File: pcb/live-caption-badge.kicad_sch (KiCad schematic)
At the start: 33 parts, among them J1 USB_C_Receptacle_USB2.0_14P, J2 Conn_01x04_Socket, J3 Conn_01x08_Socket, SW1 KILL, SW2 RST, SW3 BTN, SW4 BTN, SW5 BTN, U1 ESP32-S3-WROOM-1, U2 HE9073A33M5R, U3 HE9073A33M5R

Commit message: pcb: More layout, design 18650 battery holder footprint
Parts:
- BT1: footprint (none) -> live-caption-badge:BH-18650-B1BA002
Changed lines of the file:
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@@
 			)
 		)
-		(property "Footprint" ""
+		(property "Footprint" "live-caption-badge:BH-18650-B1BA002"
 			(at 50.8 49.276 90)
 			(effects

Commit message: pcb: I'm working in Spain but the S is silent
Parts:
- removed J1: USB_C_Receptacle_USB2.0_14P, symbol Connector:USB_C_Receptacle_USB2.0_14P
- removed J3: Conn_01x08_Socket, Connector_PinSocket_2.00mm:PinSocket_1x08_P2.00mm_Horizontal, symbol Connector:Conn_01x08_Socket
- added J3: Conn_01x09, Connector_Molex:Molex_CLIK-Mate_502386-0970_1x09-1MP_P1.25mm_Horizontal, symbol Connector_Generic:Conn_01x09
- added J5: USB_C_Receptacle_USB2.0_16P, live-caption-badge:USB_C_Receptacle_Molex_2169900002, symbol Connector:USB_C_Receptacle_USB2.0_16P
- SW3, SW4, SW5: footprint (none) -> live-caption-badge:SW_Push_TL1100CF160Q
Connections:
- net +3V3: now also J3.1 (Pin_1)
- net EPD_DC: now also J3.6 (Pin_6)
- net EPD_~{BUSY}: now also J3.8 (Pin_8)
- net EPD_~{RST}: now also J3.7 (Pin_7)
- net GND: now also J3.2 (Pin_2), J5.A1 (GND), J5.A12 (GND), J5.B1 (GND), J5.B12 (GND), J5.S1 (SHIELD)
- net SPI_CS: now also J3.5 (Pin_5)
- net SPI_MOSI: now also J3.3 (Pin_3)
- net SPI_SCK: now also J3.4 (Pin_4)
- net USB_D+: now also J5.A6 (D+), J5.B6 (D+)
- net USB_D-: now also J5.A7 (D-), J5.B7 (D-)
- net VBUS: now also J5.A4 (VBUS), J5.A9 (VBUS), J5.B4 (VBUS), J5.B9 (VBUS)
- net at R5.1: now also J5.B5 (CC2)
- net at R4.1: now also J5.A5 (CC1)
- net EPD_PWR: now reaches U1.7 (IO7)
- net EPD_PWR: now also J3.9 (Pin_9)
- no-connect marks 15 -> 16
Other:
- note added: "5V"

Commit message: pcb: 473 cannot defeat me in any way that matters
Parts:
- removed C5, C6: TBD, Capacitor_SMD:C_0603_1608Metric, symbol Device:C_Small
- removed R6, R7: 0, Resistor_SMD:R_0603_1608Metric, symbol Device:R_US
- removed SW1: KILL, symbol Switch:SW_SPDT
- added J3: Conn_01x09, Connector_PinHeader_2.54mm:PinHeader_1x09_P2.54mm_Vertical, symbol Connector_Generic:Conn_01x09
- added SW1: SW_DPDT_x2, live-caption-badge:SW_DPDT_SLW-867569-4A-N-D, symbol Switch:SW_DPDT_x2
- SW2: footprint (none) -> live-caption-badge:SW_Push_6x3mm
- renumbered J3 to J1
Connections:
- net +3V3: now also J3.1 (Pin_1)
- net +BATT: now also BT1.1 (+), SW1.1 (A); no longer C7.1, C9.1, U2.1 (IN), U2.3 (CE), U3.1 (IN), U3.3 (CE)
- net EPD_DC: now also J3.6 (Pin_6)
- net EPD_PWR: now also J3.9 (Pin_9)
- net EPD_~{BUSY}: now also J3.8 (Pin_8)
- net EPD_~{RST}: now also J3.7 (Pin_7)
- net GND: now also J3.2 (Pin_2)
- net SPI_CS: now also J3.5 (Pin_5)
- net SPI_MOSI: now also J3.3 (Pin_3)
- net SPI_SCK: now also J3.4 (Pin_4)
- net USB_D+: now also U1.14 (IO20)
- net USB_D-: now also U1.13 (IO19)
- net VBUS: now also SW1.3 (C)
- new net V_UNREG: C7.1, C9.1, SW1.2 (B), U2.1 (IN), U2.3 (CE), U3.1 (IN), U3.3 (CE)
- no-connect marks 16 -> 18
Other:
- note removed: "In case we need some lowpassing"
- moved on the sheet: BT1, C11, C12, C13, J2, R8, SW3, SW4, SW5

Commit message: pcb: pretty much done
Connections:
- net ADC_INT: now also U1.27 (IO0); no longer U1.16 (IO46)
- net AMP_CTRL: now also U1.38 (IO2); no longer U1.25 (IO48)
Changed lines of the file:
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@@
-	)
-	(no_connect
-		(at 124.46 45.72)
 	)
 	(no_connect
@@
 	)
 	(no_connect
+		(at 154.94 81.28)
+	)
+	(no_connect
 		(at 154.94 55.88)
 	)
@@
 	)
 	(no_connect
-		(at 124.46 50.8)
+		(at 154.94 86.36)
 	)
 	(no_connect
@@
 	(wire
 		(pts
-			(xy 154.94 86.36) (xy 165.1 86.36)
+			(xy 124.46 50.8) (xy 114.3 50.8)
 		)
 		(stroke
@@
 	(wire
 		(pts
-			(xy 154.94 81.28) (xy 165.1 81.28)
+			(xy 124.46 45.72) (xy 114.3 45.72)
 		)
 		(stroke
@@
 	)
 	(label "ADC_INT"
-		(at 165.1 81.28 180)
-		(fields_autoplaced yes)
-		(effects
-			(font
-				(size 1.27 1.27)
-			)
-			(justify right bottom)
+		(at 114.3 45.72 0)
+		(fields_autoplaced yes)
+		(effects
+			(font
+				(size 1.27 1.27)
+			)
+			(justify left bottom)
 		)
 	)
@@
 	)
 	(label "AMP_CTRL"
-		(at 165.1 86.36 180)
-		(fields_autoplaced yes)
-		(effects
-			(font
-				(size 1.27 1.27)
-			)
-			(justify right bottom)
-		)
-	)
+		(at 114.3 50.8 0)
+		(fields_autoplaced yes)
+		(effects
+			(font
+				(size 1.27 1.27)
+			)
+			(justify left bottom)
+		)
+	)

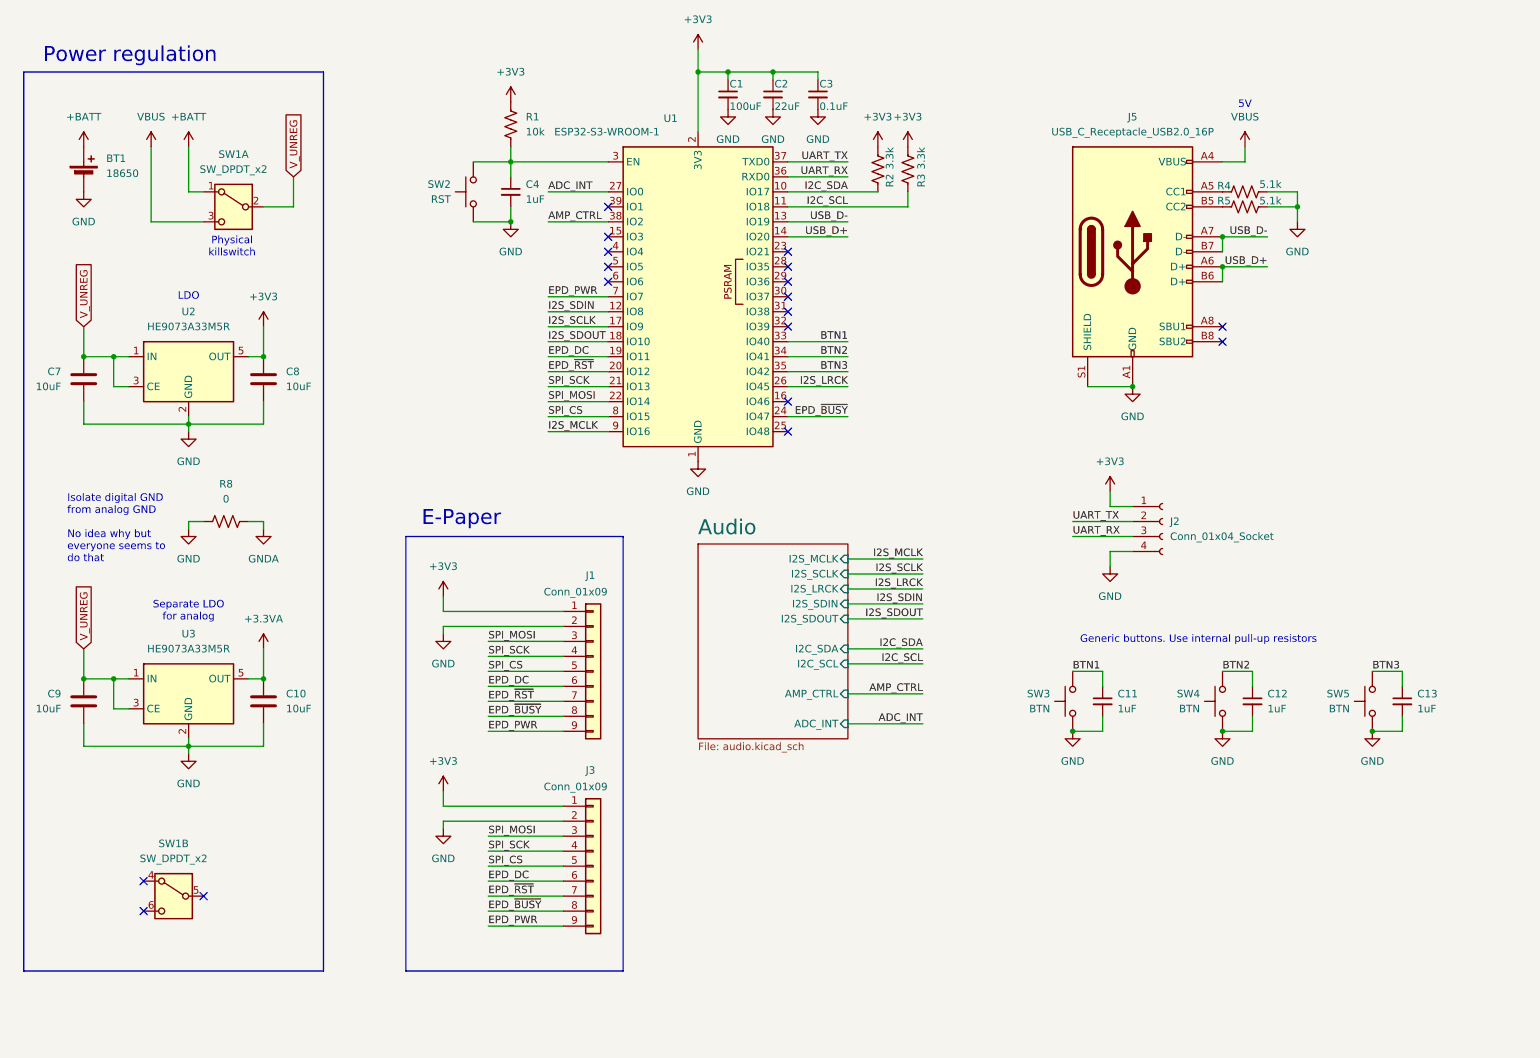
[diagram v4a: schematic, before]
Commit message: pcb: Fix misc footprints, add silkprint
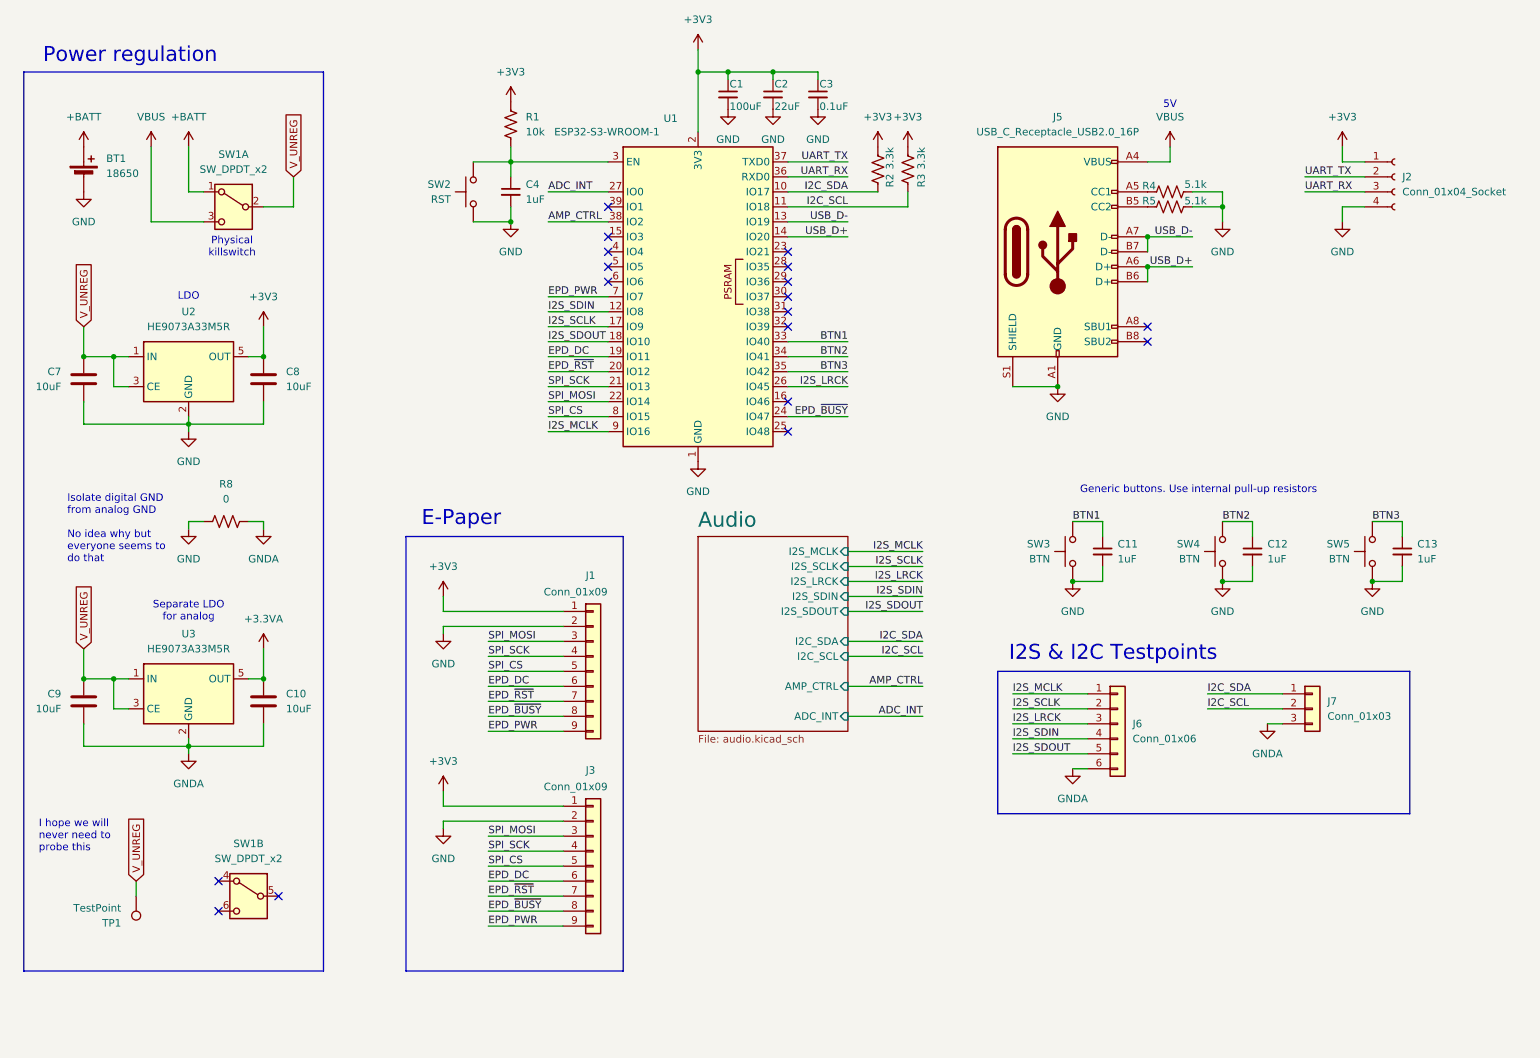
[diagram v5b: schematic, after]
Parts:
- added J6: Conn_01x06, Connector_PinHeader_2.54mm:PinHeader_1x06_P2.54mm_Vertical, symbol Connector_Generic:Conn_01x06
- added J7: Conn_01x03, Connector_PinHeader_2.54mm:PinHeader_1x03_P2.54mm_Vertical, symbol Connector_Generic:Conn_01x03
- added TP1: TestPoint, symbol Connector:TestPoint
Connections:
- net GND: no longer C10.2, C9.2, U3.2 (GND)
- net GNDA: now also C10.2, C9.2, U3.2 (GND), J6.6 (Pin_6), J7.3 (Pin_3)
- net I2C_SCL: now also J7.2 (Pin_2)
- net I2C_SDA: now also J7.1 (Pin_1)
- net I2S_LRCK: now also J6.3 (Pin_3)
- net I2S_MCLK: now also J6.1 (Pin_1)
- net I2S_SCLK: now also J6.2 (Pin_2)
- net I2S_SDIN: now also J6.4 (Pin_4)
- net I2S_SDOUT: now also J6.5 (Pin_5)
- net V_UNREG: now also TP1.1
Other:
- note added: "I hope we will never need to probe this"
- note added: "I2S & I2C Testpoints"
- moved on the sheet: C11, C12, C13, J2, J5, R4, R5, SW1B, SW3, SW4, SW5

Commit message: pcb: Checkpoint before incorporating Mark and James' suggestions
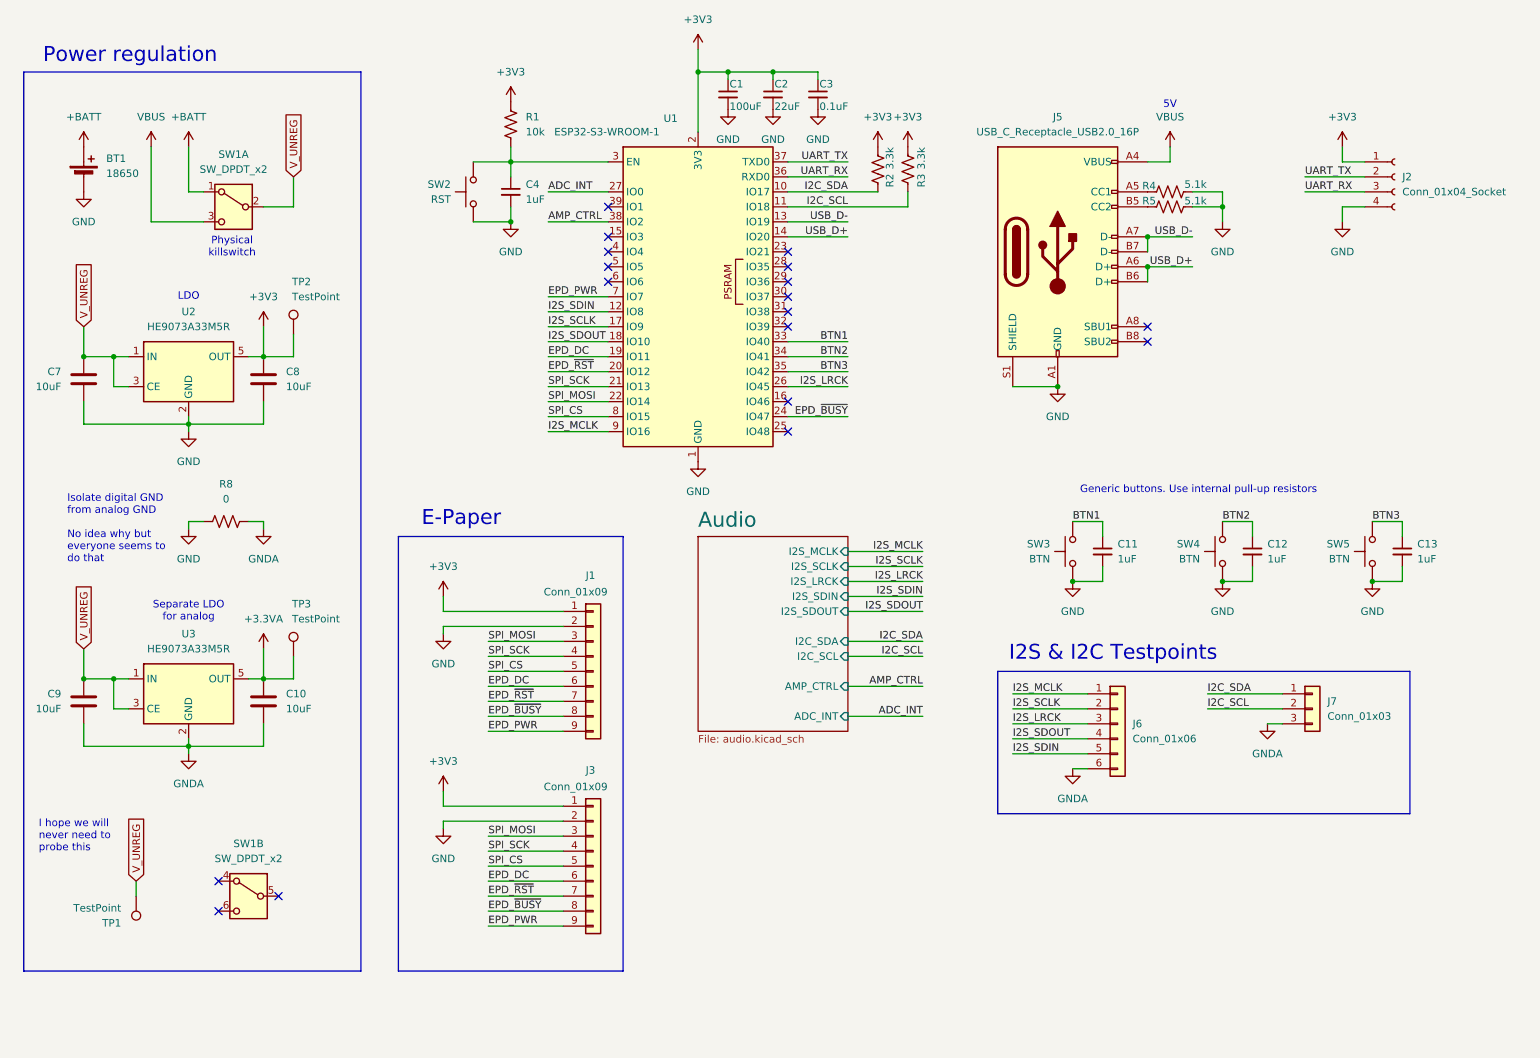
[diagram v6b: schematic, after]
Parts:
- added TP2, TP3: TestPoint, Connector_PinHeader_2.54mm:PinHeader_1x01_P2.54mm_Vertical, symbol Connector:TestPoint
- TP1: footprint (none) -> Connector_PinHeader_2.54mm:PinHeader_1x01_P2.54mm_Vertical
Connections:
- net +3.3VA: now also TP3.1
- net +3V3: now also TP2.1
- net I2S_SDIN: now also J6.5 (Pin_5); no longer J6.4 (Pin_4)
- net I2S_SDOUT: now also J6.4 (Pin_4); no longer J6.5 (Pin_5)
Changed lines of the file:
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@@
 	(wire
 		(pts
+			(xy 66.04 128.27) (xy 71.12 128.27)
+		)
+		(stroke
+			(width 0)
+			(type default)
+		)
+	)
+	(wire
+		(pts
 			(xy 96.52 119.38) (xy 96.52 120.65)
 		)
@@
 	(wire
 		(pts
+			(xy 71.12 128.27) (xy 71.12 124.46)
+		)
+		(stroke
+			(width 0)
+			(type default)
+		)
+	)
+	(wire
+		(pts
 			(xy 66.04 135.89) (xy 66.04 139.7)
 		)
@@
 	(wire
 		(pts
+			(xy 71.12 69.85) (xy 71.12 73.66)
+		)
+		(stroke
+			(width 0)
+			(type default)
+		)
+	)
+	(wire
+		(pts
 			(xy 165.1 106.68) (xy 177.8 106.68)
 		)
@@
 	(wire
 		(pts
+			(xy 71.12 73.66) (xy 66.04 73.66)
+		)
+		(stroke
+			(width 0)
+			(type default)
+		)
+	)
+	(wire
+		(pts
 			(xy 104.14 154.94) (xy 116.84 154.94)
 		)
@@
 	(rectangle
 		(start 25.4 25.4)
-		(end 76.2 177.8)
+		(end 82.55 177.8)
 		(stroke
 			(width 0)
@@
 	)
 	(rectangle
-		(start 90.17 104.14)
+		(start 88.9 104.14)
 		(end 127 177.8)
 		(stroke
@@
 	)
 	(label "I2S_SDOUT"
-		(at 193.04 140.97 0)
+		(at 193.04 138.43 0)
 		(fields_autoplaced yes)
 		(effects
@@
 	)
 	(label "I2S_SDIN"
-		(at 193.04 138.43 0)
+		(at 193.04 140.97 0)
 		(fields_autoplaced yes)
 		(effects
@@
 	)
 	(symbol
+		(lib_id "Connector:TestPoint")
+		(at 71.12 124.46 0)
+		(unit 1)
+		(exclude_from_sim no)
+		(in_bom yes)
+		(on_board yes)
+		(dnp no)
+		(property "Reference" "TP3"
+			(at 70.866 115.57 0)
+			(effects
+				(font
+					(size 1.27 1.27)
+				)
+				(justify left)
+			)
+		)
+		(property "Value" "TestPoint"
+			(at 70.866 118.11 0)
+			(effects
+				(font
+					(size 1.27 1.27)
+				)
+				(justify left)
+			)
+		)
+		(property "Footprint" "Connector_PinHeader_2.54mm:PinHeader_1x01_P2.54mm_Vertical"
+			(at 76.2 124.46 0)
+			(effects
+				(font
+					(size 1.27 1.27)
+				)
+				(hide yes)
+			)
+		)
+		(property "Datasheet" "~"
+			(at 76.2 124.46 0)
+			(effects
+				(font
+					(size 1.27 1.27)
+				)
+				(hide yes)
+			)
+		)
+		(property "Description" "test point"
+			(at 71.12 124.46 0)
+			(effects
+				(font
+					(size 1.27 1.27)
+				)
+				(hide yes)
+			)
+		)
+		(pin "1"
+		)
+		(instances
+			(project "live-caption-badge"
+				(path "/3b930924-1452-4d23-815e-09afbcdc5905"
+					(reference "TP3")
+					(unit 1)
+				)
+			)
+		)
+	)
+	(symbol
 		(lib_id "Device:Battery_Cell")
 		(at 35.56 43.18 0)
@@
 			)
 		)
-		(property "Footprint" ""
+		(property "Footprint" "Connector_PinHeader_2.54mm:PinHeader_1x01_P2.54mm_Vertical"
 			(at 39.37 165.1 0)
 			(effects
@@
 					(unit 1)
 				)
+			)
+		)
+	)
+	(symbol
+		(lib_id "Connector:TestPoint")
+		(at 71.12 69.85 0)
+		(unit 1)
+		(exclude_from_sim no)
+		(in_bom yes)
+		(on_board yes)
+		(dnp no)
+		(property "Reference" "TP2"
+			(at 70.866 60.96 0)
+			(effects
+				(font
+					(size 1.27 1.27)
+				)
+				(justify left)
+			)
+		)
+		(property "Value" "TestPoint"
+			(at 70.866 63.5 0)
+			(effects
+				(font
+					(size 1.27 1.27)
+				)
+				(justify left)
+			)
+		)
+		(property "Footprint" "Connector_PinHeader_2.54mm:PinHeader_1x01_P2.54mm_Vertical"
+			(at 76.2 69.85 0)
+			(effects
+				(font
+					(size 1.27 1.27)
+				)
+				(hide yes)
+			)
+		)
+		(property "Datasheet" "~"
+			(at 76.2 69.85 0)
+			(effects
+				(font
+					(size 1.27 1.27)
+				)
+				(hide yes)
+			)
+		)
+		(property "Description" "test point"
+			(at 71.12 69.85 0)
+			(effects
+				(font
+					(size 1.27 1.27)
+				)
+				(hide yes)
+			)
+		)
+		(pin "1"
+		)
+		(instances
+			(project "live-caption-badge"
+				(path "/3b930924-1452-4d23-815e-09afbcdc5905"
+					(reference "TP2")
+					(unit 1)
+				)
